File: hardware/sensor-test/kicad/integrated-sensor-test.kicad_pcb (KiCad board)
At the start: 4 copper layers, 110 x 75 mm, 77 parts, among them J1 TYPE-C-31-M-12, J2 Conn_01x02, U1 RP2040, U10 USBLC6-2SC6, U2 W25Q16JVUXIQ, U3 AP2112K-3.3TRG1, U4 TPS22919DCKR, U5 TMUX1208PWR, U6 DRV5055A3QDBZR, U7 DRV5055A3QDBZR, U8 DRV5055A3QDBZR, U9 DRV5055A3QDBZR, Y1 ABM8-272-T3

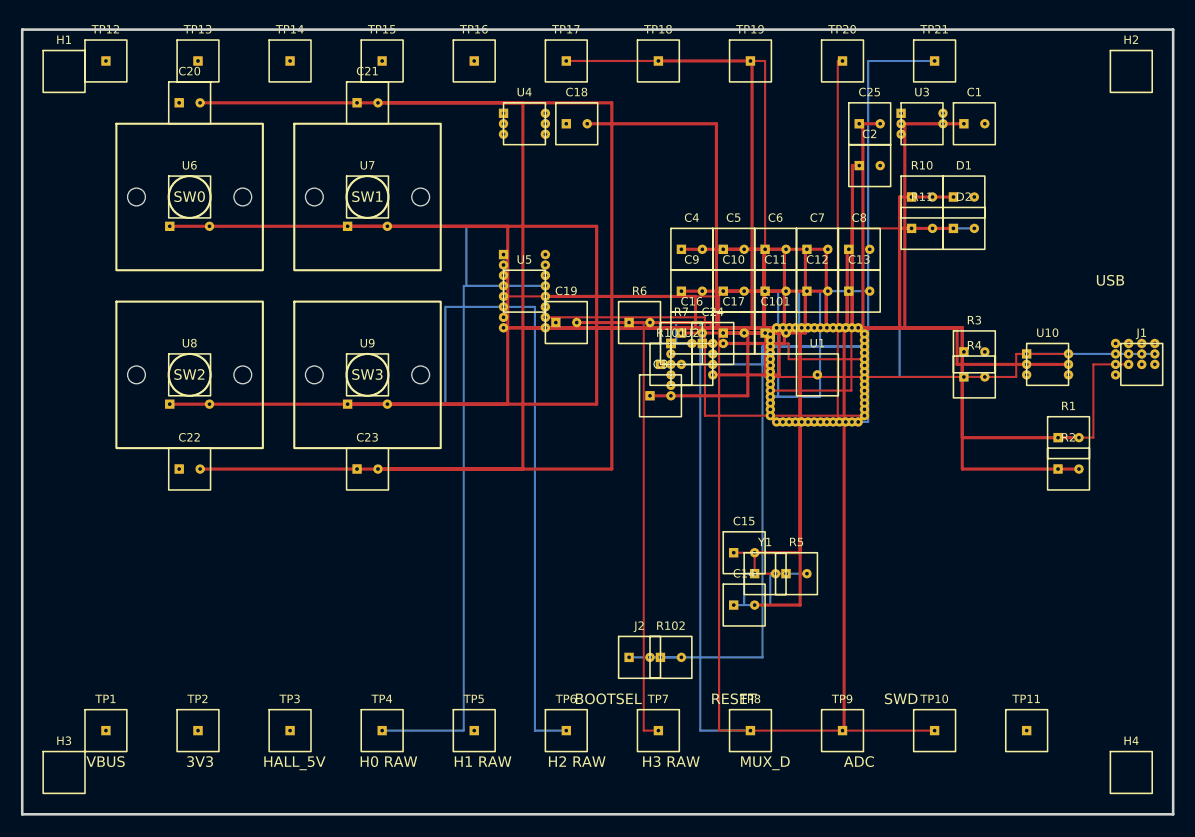
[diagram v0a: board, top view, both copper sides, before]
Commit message: Rework PCB routing with surface-mount pads and vias
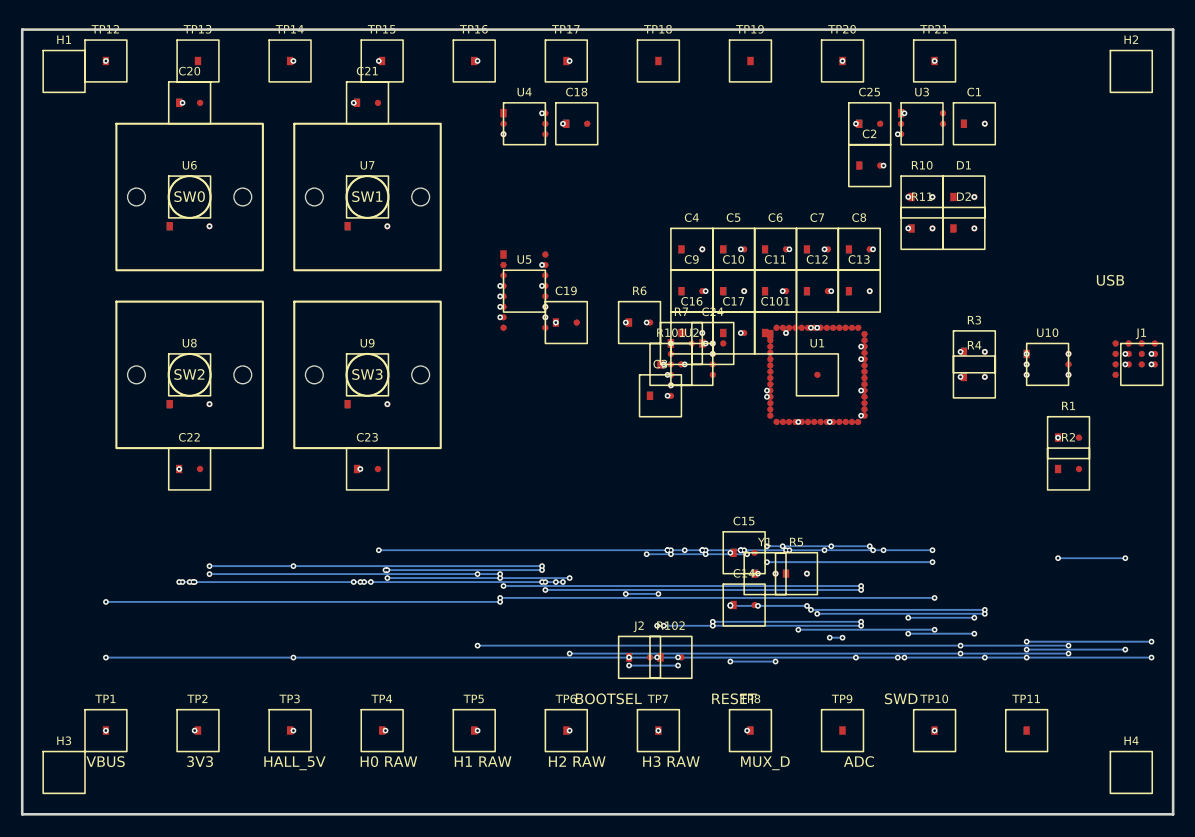
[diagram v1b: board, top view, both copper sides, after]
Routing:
- net GND: track 1238.9 -> 0.00 mm
- net +3V3: track 318.6 -> 494.4 mm, vias 0 -> 34
- net PWR_LED_A: track 6.00 -> 87.1 mm, vias 0 -> 4
- net USB_D+_PROTECTED: track 86.8 -> 167.0 mm, vias 0 -> 6
- net USB_D-_PROTECTED: track 80.4 -> 160.0 mm, vias 0 -> 6
- net STATUS_LED_A: track 6.00 -> 84.1 mm, vias 0 -> 4
- net HALL_5V: track 483.1 -> 415.5 mm, vias 0 -> 26
- net MUX_S7_SPARE: track 59.5 -> 119.9 mm, vias 0 -> 4
- net USB_D+_CONN: track 12.2 -> 67.2 mm, vias 0 -> 4
- net USB_D-_CONN: track 11.8 -> 64.3 mm, vias 0 -> 4
- net +1V1: track 46.8 -> 98.2 mm, vias 0 -> 8
- net Net-(U1-Pad41): track 18.0 -> 68.7 mm, vias 0 -> 4
- net QSPI_SD3: track 16.0 -> 66.2 mm, vias 0 -> 4
- net Net-(U1-Pad40): track 21.0 -> 66.2 mm, vias 0 -> 4
- net SWCLK: track 35.4 -> 77.3 mm, vias 0 -> 4
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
